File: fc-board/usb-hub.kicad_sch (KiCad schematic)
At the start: 22 parts, among them J3 M80-5322042, U6 USB2517I-JZX, Y1 ECS-3963-240-BN-TR

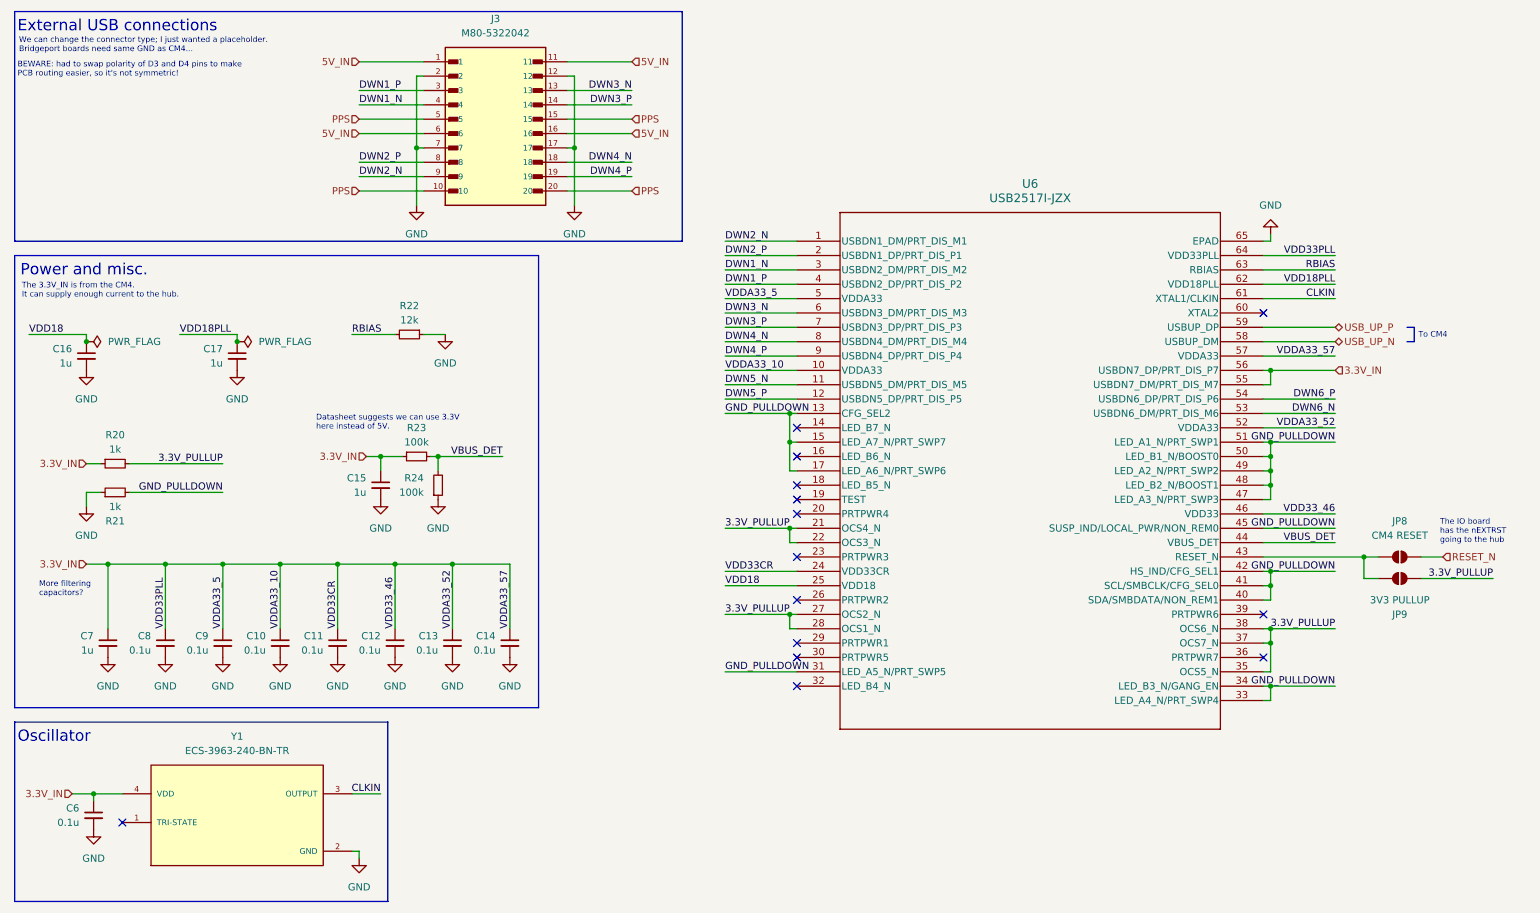
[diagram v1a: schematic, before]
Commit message: Removed zips; updated gitignore
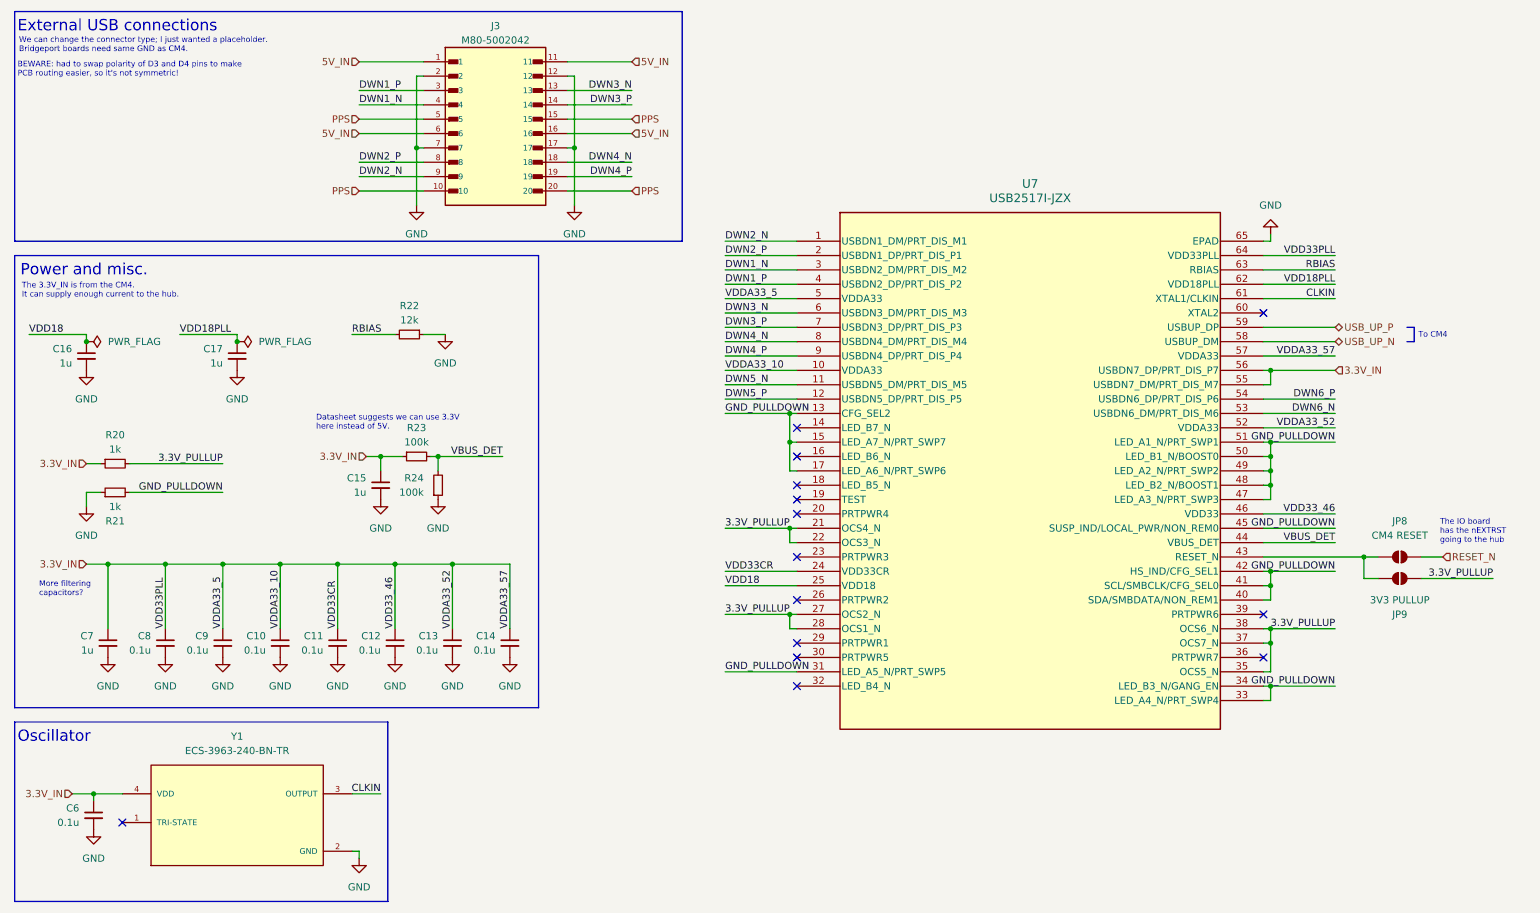
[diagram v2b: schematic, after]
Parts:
- removed J3: M80-5322042, fc-board:M80-5322042, symbol fc-board:M80-5322042
- added J3: M80-5002042, fc-board:M80-5002042, symbol fc-board:M80-5002042
- renumbered U6 to U7
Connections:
- net 5V_IN: now also J3.1, J3.11, J3.16, J3.6
- net DWN1_N: now also J3.4
- net DWN1_P: now also J3.3
- net DWN2_N: now also J3.9
- net DWN2_P: now also J3.8
- net DWN3_N: now also J3.13
- net DWN3_P: now also J3.14
- net DWN4_N: now also J3.18
- net DWN4_P: now also J3.19
- net GND: now also J3.12, J3.17, J3.2, J3.7
- net PPS: now also J3.10, J3.15, J3.20, J3.5
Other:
- note added: "We can change the connector type; I just wanted a placeholder. Bridgeport boards need same GND as CM4."
- note removed: "We can change the connector type; I just wanted a placeholder. Bridgeport boards need same GND as CM4..."
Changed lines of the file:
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@@
 		)
 	)
-	(text "We can change the connector type; I just wanted a placeholder.\nBridgeport boards need same GND as CM4..."
+	(text "We can change the connector type; I just wanted a placeholder.\nBridgeport boards need same GND as CM4."
 		(exclude_from_sim no)
 		(at 16.002 22.606 0)
@@
 	)
 	(symbol
+		(lib_id "fc-board:M80-5002042")
+		(at 100.33 36.83 0)
+		(unit 1)
+		(exclude_from_sim no)
+		(in_bom yes)
+		(on_board yes)
+		(dnp no)
+		(fields_autoplaced yes)
+		(property "Reference" "J3"
+			(at 100.33 17.78 0)
+			(effects
+				(font
+					(size 1.27 1.27)
+				)
+			)
+		)
+		(property "Value" "M80-5002042"
+			(at 100.33 20.32 0)
+			(effects
+				(font
+					(size 1.27 1.27)
+				)
+			)
+		)
+		(property "Footprint" "fc-board:M80-5002042"
+			(at 99.822 13.716 0)
+			(effects
+				(font
+					(size 1.27 1.27)
+				)
+				(justify bottom)
+				(hide yes)
+			)
+		)
+		(property "Datasheet" ""
+			(at 100.33 36.83 0)
+			(effects
+				(font
+					(size 1.27 1.27)
+				)
+				(hide yes)
+			)
+		)
+		(property "Description" ""
+			(at 100.33 36.83 0)
+			(effects
+				(font
+					(size 1.27 1.27)
+				)
+				(hide yes)
+			)
+		)
+		(property "MANUFACTURER" "HARWIN"
+			(at 100.33 36.83 0)
+			(effects
+				(font
+					(size 1.27 1.27)
+				)
+				(justify bottom)
+				(hide yes)
+			)
+		)
+		(pin "14"
+		)
+		(pin "13"
+		)
+		(pin "3"
+		)
+		(pin "16"
+		)
+		(pin "17"
+		)
+		(pin "2"
+		)
+		(pin "18"
+		)
+		(pin "8"
+		)
+		(pin "1"
+		)
+		(pin "15"
+		)
+		(pin "10"
+		)
+		(pin "12"
+		)
+		(pin "20"
+		)
+		(pin "9"
+		)
+		(pin "4"
+		)
+		(pin "7"
+		)
+		(pin "6"
+		)
+		(pin "5"
+		)
+		(pin "19"
+		)
+		(pin "11"
+		)
+		(instances
+			(project ""
+				(path "/14bbabed-904f-4efc-8ba4-be00e59385c4/8fd07369-1c3f-41cf-a32e-88b0d98439a9"
+					(reference "J3")
+					(unit 1)
+				)
+			)
+		)
+	)
+	(symbol
 		(lib_id "fc-board:ECS-3963-240-BN-TR")
 		(at 54.61 156.21 0)
@@
 		(dnp no)
 		(fields_autoplaced yes)
-		(property "Reference" "U6"
+		(property "Reference" "U7"
 			(at 194.945 45.72 0)
 			(effects
@@
 			(project ""
 				(path "/14bbabed-904f-4efc-8ba4-be00e59385c4/8fd07369-1c3f-41cf-a32e-88b0d98439a9"
-					(reference "U6")
+					(reference "U7")
 					(unit 1)
 				)
@@
 					(unit 1)
 				)
-			)
-		)
-	)
-	(symbol
-		(lib_id "fc-board:M80-5322042")
-		(at 100.33 36.83 0)
-		(unit 1)
-		(exclude_from_sim no)
-		(in_bom yes)
-		(on_board yes)
-		(dnp no)
-		(fields_autoplaced yes)
-		(property "Reference" "J3"
-			(at 100.33 16.51 0)
-			(effects
-				(font
-					(size 1.27 1.27)
-				)
-			)
-		)
-		(property "Value" "M80-5322042"
-			(at 100.33 19.05 0)
-			(effects
-				(font
-					(size 1.27 1.27)
-				)
-			)
-		)
-		(property "Footprint" "fc-board:M80-5322042"
-			(at 100.33 36.83 0)
-			(effects
-				(font
-					(size 1.27 1.27)
-				)
-				(justify bottom)
-				(hide yes)
-			)
-		)
-		(property "Datasheet" ""
-			(at 100.33 36.83 0)
-			(effects
-				(font
-					(size 1.27 1.27)
-				)
-				(hide yes)
-			)
-		)
-		(property "Description" ""
-			(at 100.33 36.83 0)
-			(effects
-				(font
-					(size 1.27 1.27)
-				)
-				(hide yes)
-			)
-		)
-		(property "MANUFACTURER" "HARWIN"
-			(at 100.33 36.83 0)
-			(effects
-				(font
-					(size 1.27 1.27)
-				)
-				(justify bottom)
-				(hide yes)
-			)
-		)
-		(pin "18"
-		)
-		(pin "16"
-		)
-		(pin "9"
-		)
-		(pin "11"
-		)
-		(pin "1"
-		)
-		(pin "14"
-		)
-		(pin "19"
-		)
-		(pin "6"
-		)
-		(pin "2"
-		)
-		(pin "5"
-		)
-		(pin "4"
-		)
-		(pin "20"
-		)
-		(pin "3"
-		)
-		(pin "10"
-		)
-		(pin "12"
-		)
-		(pin "7"
-		)
-		(pin "13"
-		)
-		(pin "8"
-		)
-		(pin "17"
-		)
-		(pin "15"
-		)
-		(instances
-			(project "fc-board"
-				(path "/14bbabed-904f-4efc-8ba4-be00e59385c4/8fd07369-1c3f-41cf-a32e-88b0d98439a9"
-					(reference "J3")
-					(unit 1)
-				)
